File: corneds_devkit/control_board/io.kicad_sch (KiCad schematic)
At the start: 1 part, among them J1 JTAG

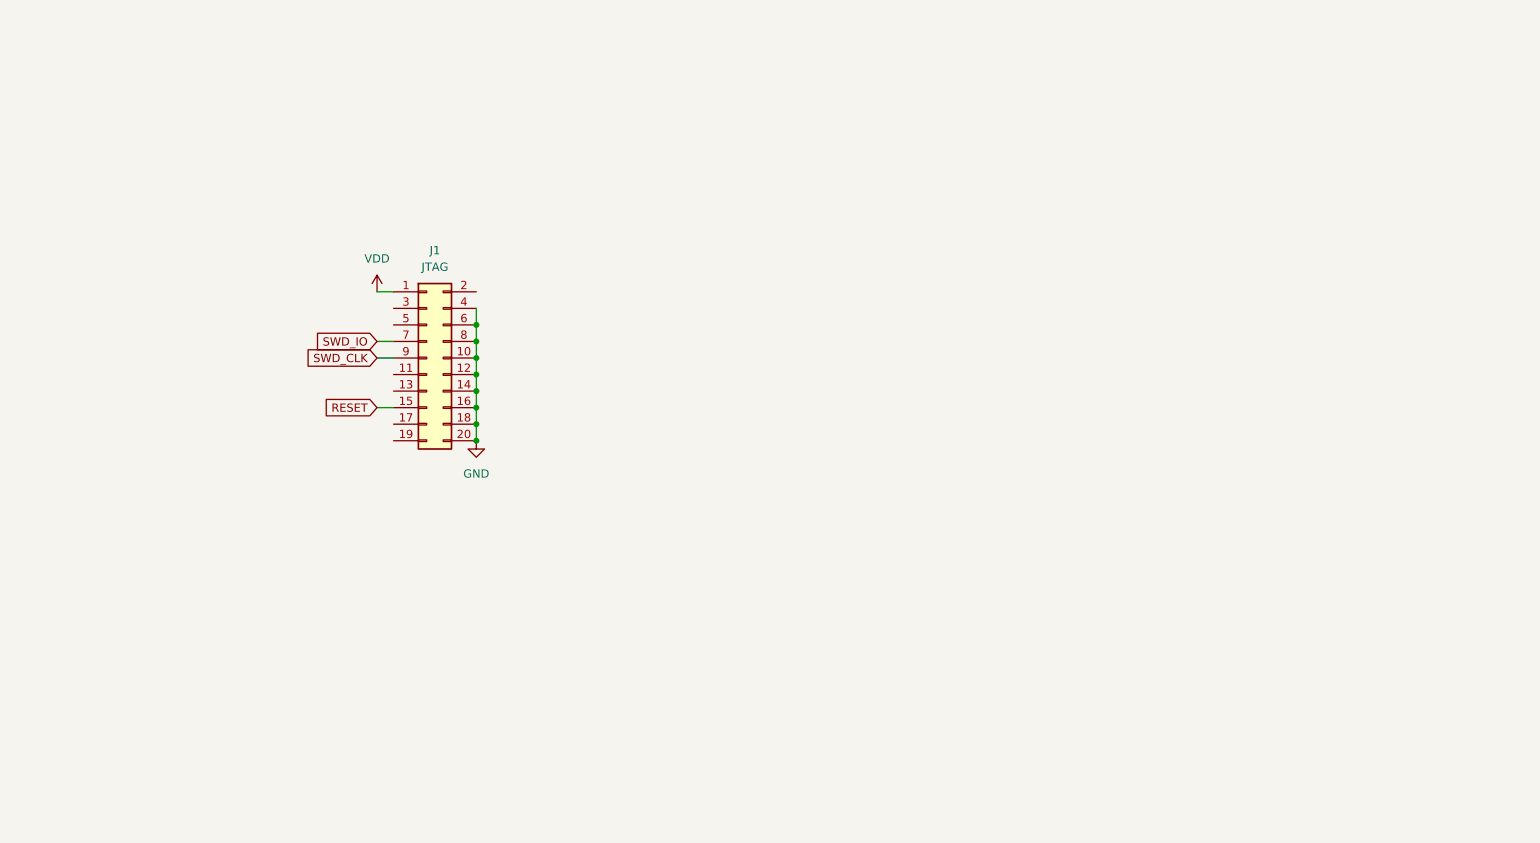
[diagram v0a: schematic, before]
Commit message: finished routing power board and started on control board schematic but realized I need seperate reset lines
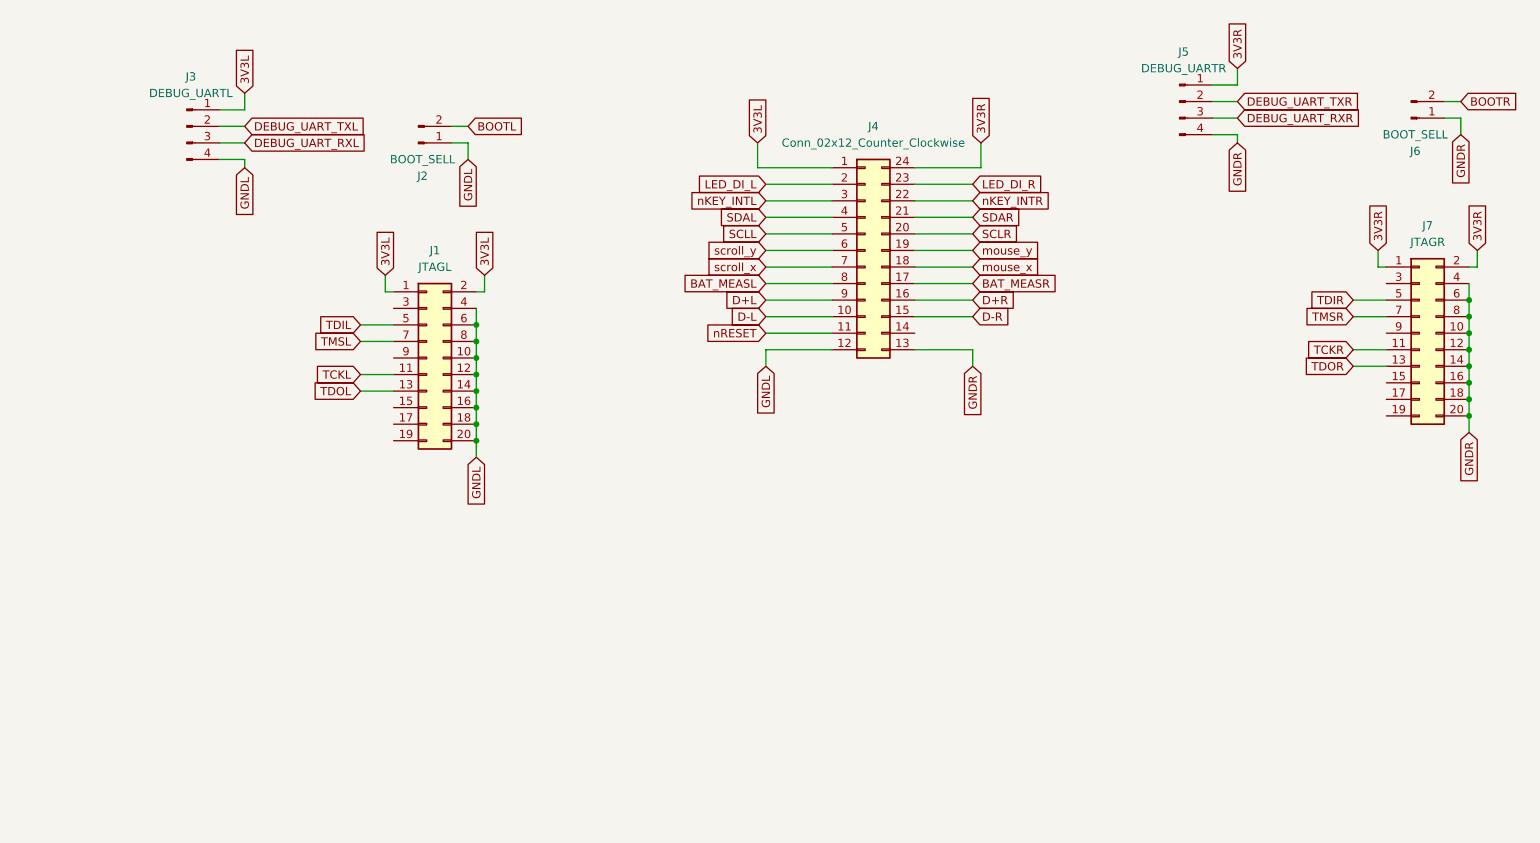
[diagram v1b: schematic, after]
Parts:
- added J2, J6: BOOT_SELL, Connector_PinHeader_1.27mm:PinHeader_1x02_P1.27mm_Vertical, symbol Connector:Conn_01x02_Pin
- added J3: DEBUG_UARTL, Connector_PinHeader_1.27mm:PinHeader_1x04_P1.27mm_Vertical, symbol Connector:Conn_01x04_Pin
- added J4: Conn_02x12_Counter_Clockwise, symbol Connector_Generic:Conn_02x12_Counter_Clockwise
- added J5: DEBUG_UARTR, Connector_PinHeader_1.27mm:PinHeader_1x04_P1.27mm_Vertical, symbol Connector:Conn_01x04_Pin
- added J7: JTAGR, symbol Connector_Generic:Conn_02x10_Odd_Even
- J1: value JTAG -> JTAGL
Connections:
- net VDD is gone; now on net 3V3L: J1.1 (Pin_1)
- net TCKL: now reaches J1.11 (Pin_11)
- net TDOL: now reaches J1.13 (Pin_13)
- net 3V3L: now reaches J1.2 (Pin_2)
- net 3V3L: now also J3.1 (Pin_1), J4.1 (Pin_1)
- net TDIL: now reaches J1.5 (Pin_5)
- net GND renamed GNDL
- net GNDL: now also J2.1 (Pin_1), J3.4 (Pin_4), J4.12 (Pin_12)
- net RESET: no longer names the net of J1.15 (Pin_15)
- net SWD_CLK: no longer names the net of J1.9 (Pin_9)
- net SWD_IO renamed TMSL
- new net 3V3R: J4.24 (Pin_24), J5.1 (Pin_1), J7.1 (Pin_1), J7.2 (Pin_2)
- new net BAT_MEASL: J4.8 (Pin_8)
- new net BAT_MEASR: J4.17 (Pin_17)
- new net BOOTL: J2.2 (Pin_2)
- new net BOOTR: J6.2 (Pin_2)
- new net D+L: J4.9 (Pin_9)
- new net D+R: J4.16 (Pin_16)
- new net D-L: J4.10 (Pin_10)
- new net D-R: J4.15 (Pin_15)
- new net DEBUG_UART_RXL: J3.3 (Pin_3)
- new net DEBUG_UART_RXR: J5.3 (Pin_3)
- new net DEBUG_UART_TXL: J3.2 (Pin_2)
- new net DEBUG_UART_TXR: J5.2 (Pin_2)
- new net GNDR: J4.13 (Pin_13), J5.4 (Pin_4), J6.1 (Pin_1), J7.10 (Pin_10), J7.12 (Pin_12), J7.14 (Pin_14), J7.16 (Pin_16), J7.18 (Pin_18), J7.20 (Pin_20), J7.4 (Pin_4), J7.6 (Pin_6), J7.8 (Pin_8)
- new net LED_DI_L: J4.2 (Pin_2)
- new net LED_DI_R: J4.23 (Pin_23)
- new net SCLL: J4.5 (Pin_5)
- new net SCLR: J4.20 (Pin_20)
- new net SDAL: J4.4 (Pin_4)
- new net SDAR: J4.21 (Pin_21)
- new net TCKR: J7.11 (Pin_11)
- new net TDIR: J7.5 (Pin_5)
- new net TDOR: J7.13 (Pin_13)
- new net TMSR: J7.7 (Pin_7)
- new net mouse_x: J4.18 (Pin_18)
- new net mouse_y: J4.19 (Pin_19)
- new net nKEY_INTL: J4.3 (Pin_3)
- new net nKEY_INTR: J4.22 (Pin_22)
- new net nRESET: J4.11 (Pin_11)
- new net scroll_x: J4.7 (Pin_7)
- new net scroll_y: J4.6 (Pin_6)

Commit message: ordered devkit rev A
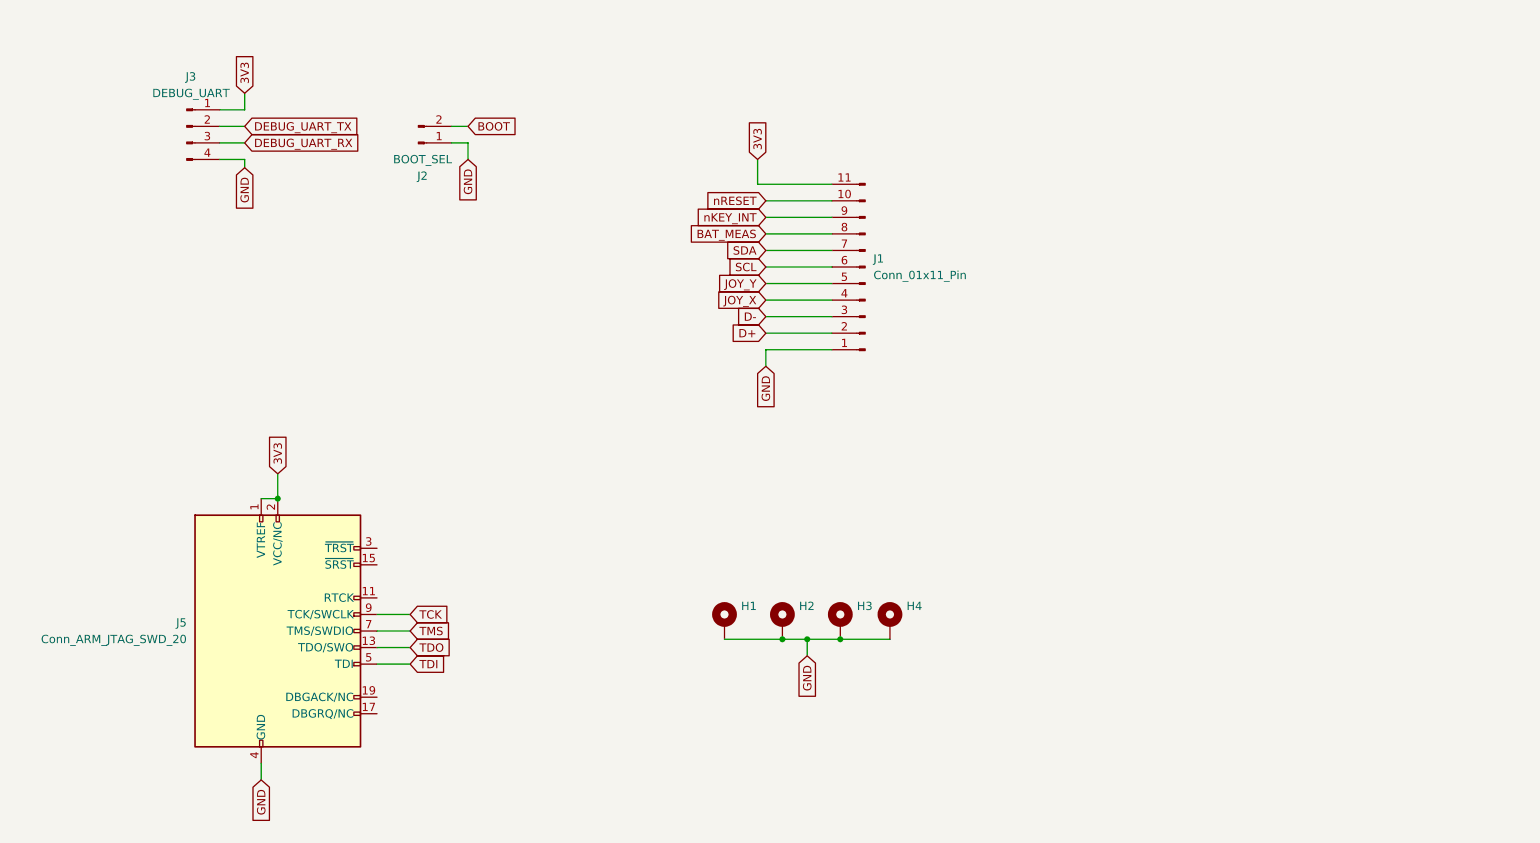
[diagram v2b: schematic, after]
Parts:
- removed J1: JTAGL, symbol Connector_Generic:Conn_02x10_Odd_Even
- removed J4: Conn_02x12_Counter_Clockwise, symbol Connector_Generic:Conn_02x12_Counter_Clockwise
- removed J5: DEBUG_UARTR, Connector_PinHeader_1.27mm:PinHeader_1x04_P1.27mm_Vertical, symbol Connector:Conn_01x04_Pin
- removed J6: BOOT_SELL, Connector_PinHeader_1.27mm:PinHeader_1x02_P1.27mm_Vertical, symbol Connector:Conn_01x02_Pin
- removed J7: JTAGR, symbol Connector_Generic:Conn_02x10_Odd_Even
- added H1, H2, H3, H4: ~, MountingHole:MountingHole_3.2mm_M3_Pad_Via, symbol Mechanical:MountingHole_Pad
- added J1: Conn_01x11_Pin, Connector_PinHeader_1.27mm:PinHeader_1x11_P1.27mm_Vertical, symbol Connector:Conn_01x11_Pin
- added J5: Conn_ARM_JTAG_SWD_20, entropy:CONN_7024620xx_MOL, symbol Connector:Conn_ARM_JTAG_SWD_20
- J2: value BOOT_SELL -> BOOT_SEL
- J3: value DEBUG_UARTL -> DEBUG_UART
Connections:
- net nRESET: now also J1.10 (Pin_10)
- net 3V3L renamed 3V3
- net 3V3: now also J1.11 (Pin_11), J5.1 (VTREF), J5.2 (VCC/NC)
- net BOOTL renamed BOOT
- net DEBUG_UART_RXL renamed DEBUG_UART_RX
- net DEBUG_UART_TXL renamed DEBUG_UART_TX
- net GNDL renamed GND
- net GND: now also H1.1, H2.1, H3.1, H4.1, J1.1 (Pin_1), J5.10 (GND), J5.12 (GND), J5.14 (GND), J5.16 (GND), J5.18 (GND), J5.20 (GND), J5.4 (GND), J5.6 (GND), J5.8 (GND)
- new net BAT_MEAS: J1.8 (Pin_8)
- new net D+: J1.2 (Pin_2)
- new net D-: J1.3 (Pin_3)
- new net JOY_X: J1.4 (Pin_4)
- new net JOY_Y: J1.5 (Pin_5)
- new net SCL: J1.6 (Pin_6)
- new net SDA: J1.7 (Pin_7)
- new net TCK: J5.9 (TCK/SWCLK)
- new net TDI: J5.5 (TDI)
- new net TDO: J5.13 (TDO/SWO)
- new net TMS: J5.7 (TMS/SWDIO)
- new net nKEY_INT: J1.9 (Pin_9)
